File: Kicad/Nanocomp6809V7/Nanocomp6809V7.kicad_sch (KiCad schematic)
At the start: 77 parts, among them J1 TTL_USB_Serial_FT232R, J2 DB15_Female_HighDensity, J3 Conn_01x15_Male, SW1 R, SW10 0, SW11 3, SW12 2, SW13 D, SW14 C, SW15 B, SW16 A, SW17 1, SW18 4, SW19 7, SW2 F, SW20 G, SW21 CN, SW22 S, SW23 L, SW24 RST, SW25 AB, SW3 6, SW4 5, SW5 M, SW6 E, SW7 9, SW8 8, SW9 I, U1 MC6809, U10 74LS92, U11 MC6850, U12 74LS245, U13 74LS541BB, U14 74LS541BB, U15 74LS541BB, U16 74LS241BB, U17 74LS157BB, U18 74LS166BB, U19 74LS04, U2 ATF22LV10, U20 REN7134-Memory_RAM, U21 74LS163-74xx, U22 74LS10, U23 MC6845BB, U24 REN7134-Memory_RAM, U3 28C64B, U4 AS6C1008, U5 6821_BBPIN, U6 7_Segment_x_4_LED_Nanocomp_RH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, U7 ULN2803A, U8 74LS145, U9 7_Segment_x_4_LED_Nanocomp, Y1 4Mhz, Y2 MXO45HS-3C-3M6862, Y3 MXO45HS-3C-25M1750

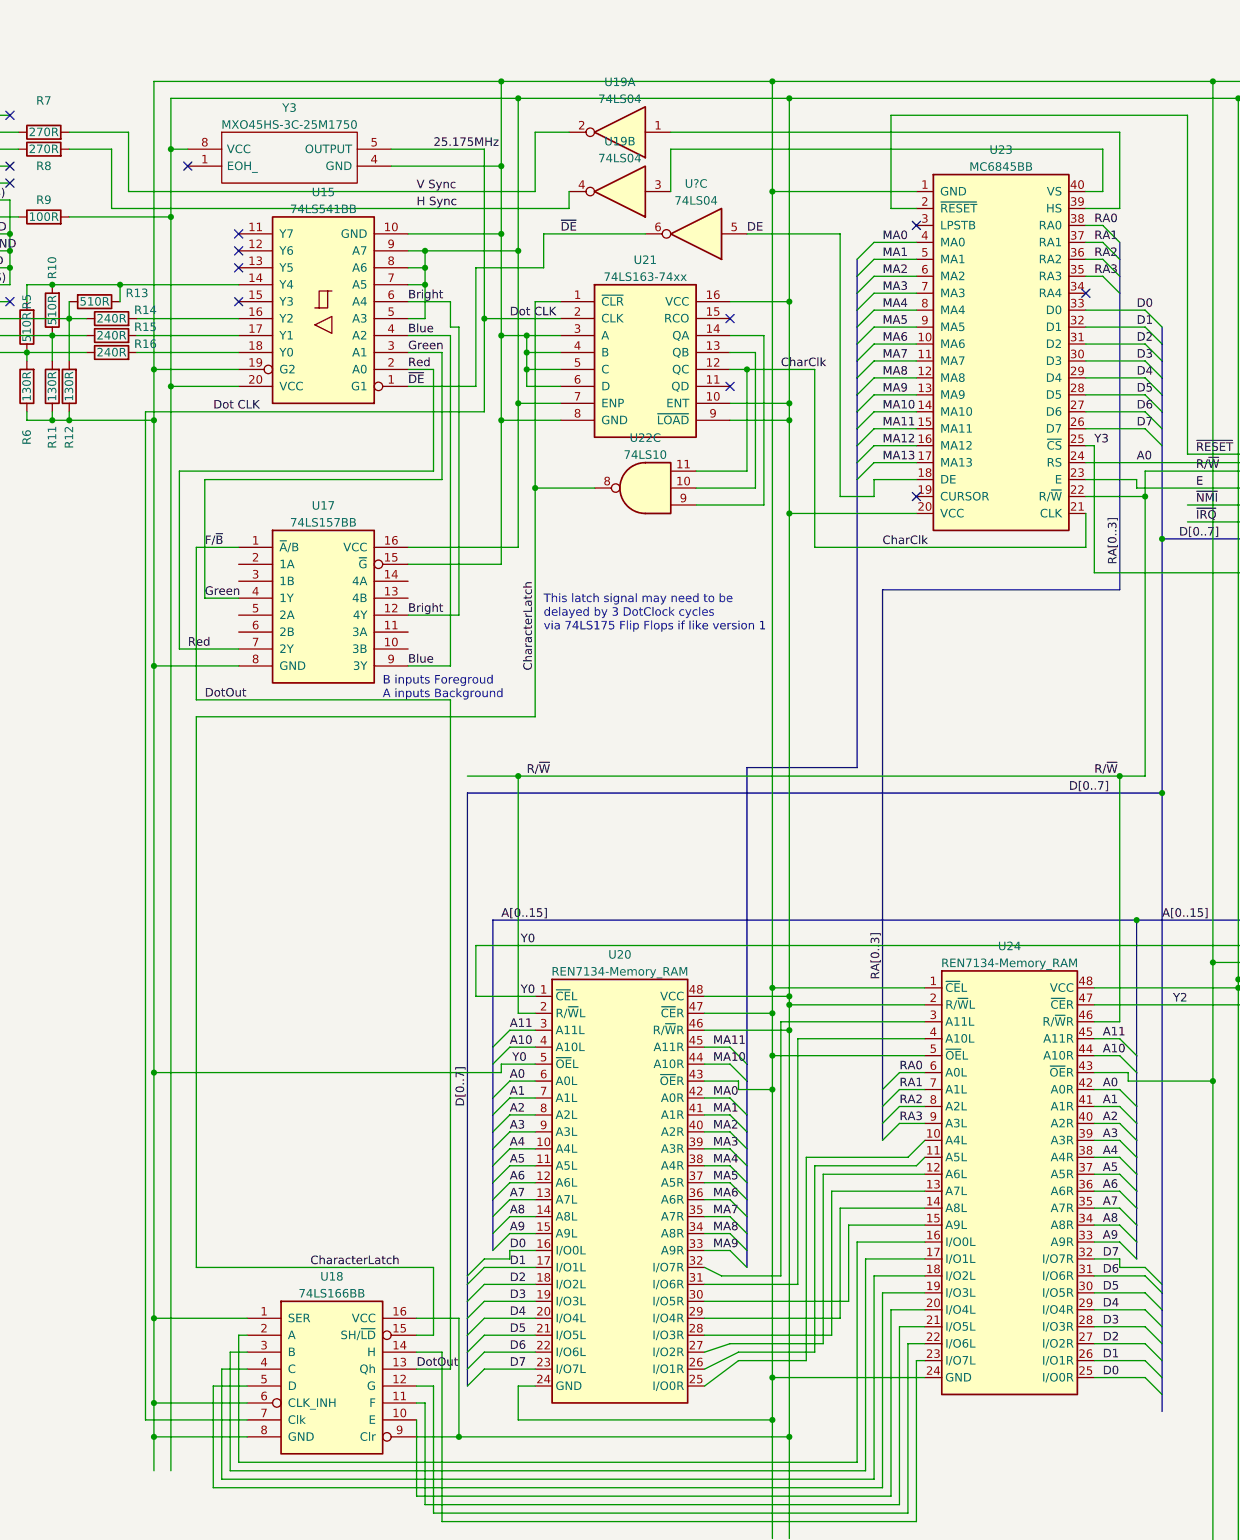
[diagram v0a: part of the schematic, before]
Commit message: Updated for Videos V04 & V05 Timing  & PLD
Updated with V6 and V7 Schematics with Timing enhancements then placement of 6 logic chips with 1 PLD/GAL
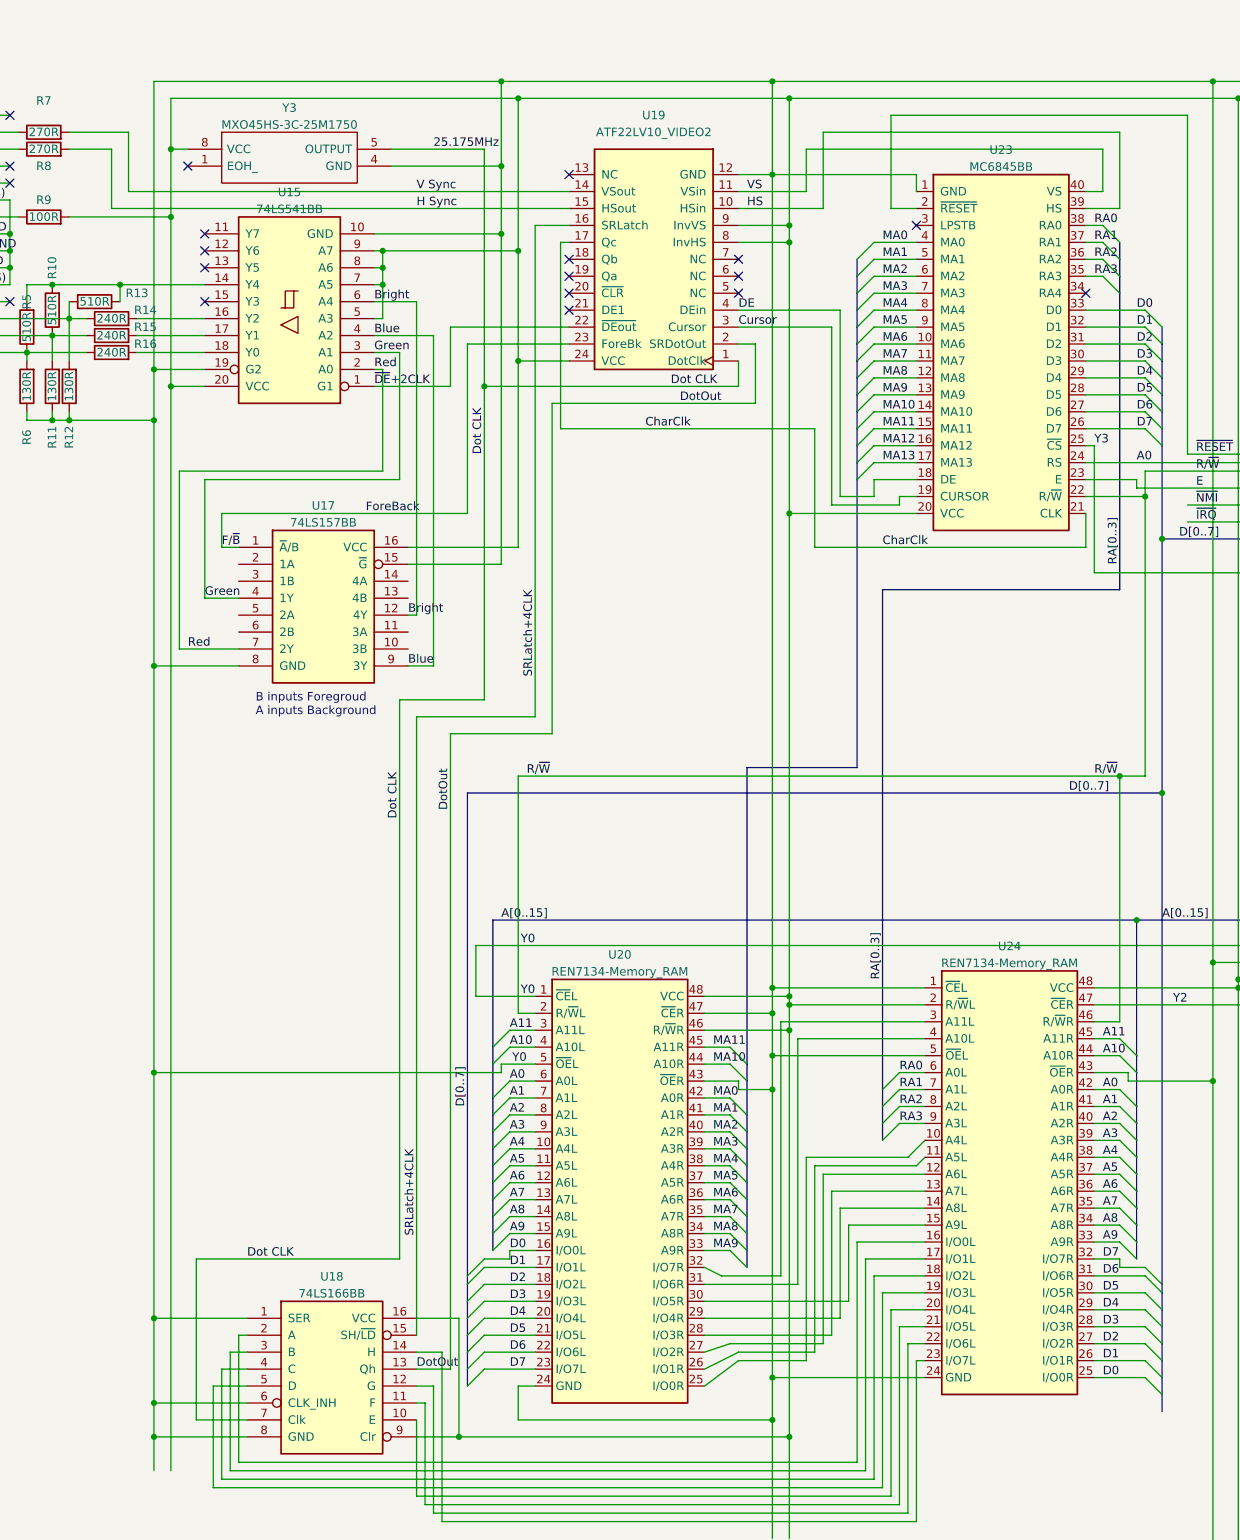
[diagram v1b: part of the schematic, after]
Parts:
- removed U19, U?: 74LS04, symbol 74xx:74LS04
- removed U21: 74LS163-74xx, symbol Breadboarding:74LS163-74xx
- removed U22: 74LS10, symbol 74xx:74LS10
- added U19: ATF22LV10_VIDEO2, symbol Breadboarding:ATF22LV10_VIDEO2
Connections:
- net 25.175MHz: now also U19.1 (DotClk)
- net CharClk: now also U19.17 (Qc)
- net DE: now also U19.4 (DEin)
- net DotOut: now also U19.2 (SRDotOut); no longer R10.1, R11.2, R15.1, U15.3 (A1), U17.1 (~{A}/B), U17.4 (1Y)
- net GND: now also U19.12 (GND)
- net H Sync: now also U19.15 (HSout)
- net V Sync: now also U19.14 (VSout)
- net VCC: now also U19.24 (VCC), U19.8 (InvHS), U19.9 (InvVS)
- net Cursor: now reaches U23.19 (CURSOR)
- net Cursor: now also U19.3 (Cursor)
- net HS: now reaches U23.39 (HS)
- net HS: now also U19.10 (HSin)
- net VS: now reaches U23.40 (VS)
- net VS: now also U19.11 (VSin)
- net CharacterLatch renamed SRLatch+4CLK
- net SRLatch+4CLK: now also U19.16 (SRLatch)
- net ~{DE} renamed ~{DE}+2CLK
- net ~{DE}+2CLK: now also U19.22 (~{DEout})
- new net ForeBack: U17.1 (~{A}/B), U19.23 (ForeBk)
- new net Green: R10.1, R11.2, R15.1, U15.3 (A1), U17.4 (1Y)
- no-connect marks 46 -> 51
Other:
- note removed: "This latch signal may need to be delayed by 3 DotClock cycles via 74LS175 Flip Flops if like version 1"
- moved on the sheet: U15
